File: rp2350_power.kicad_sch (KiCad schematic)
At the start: 24 parts, among them J1 TYPE-C 16PLT-H10.0, U2 LM2596S-3.3, U6 XXL1509-5.0

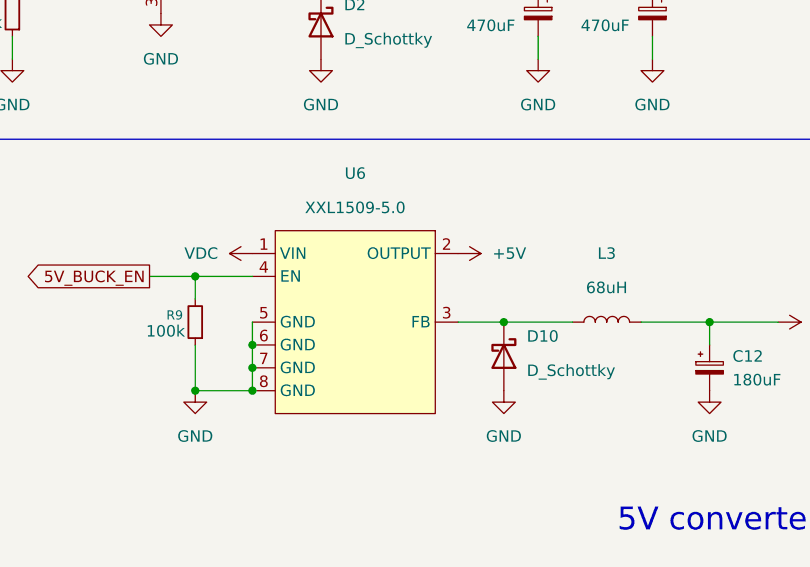
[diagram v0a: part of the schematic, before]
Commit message: fixed wrong wiring of 5V regulator for rp mcu + added all usb a ports
Signed-off-by: Toby Cm <toby@vsus.app>
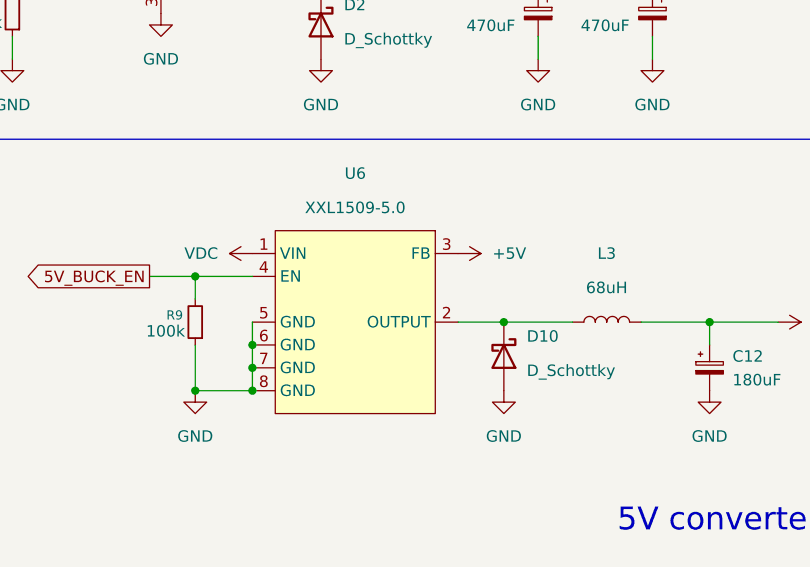
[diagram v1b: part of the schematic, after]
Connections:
- net +5V: now also U6.3 (FB); no longer U6.2 (OUTPUT)
- net at D10.1 (K), L3.1: now also U6.2 (OUTPUT); no longer U6.3 (FB)

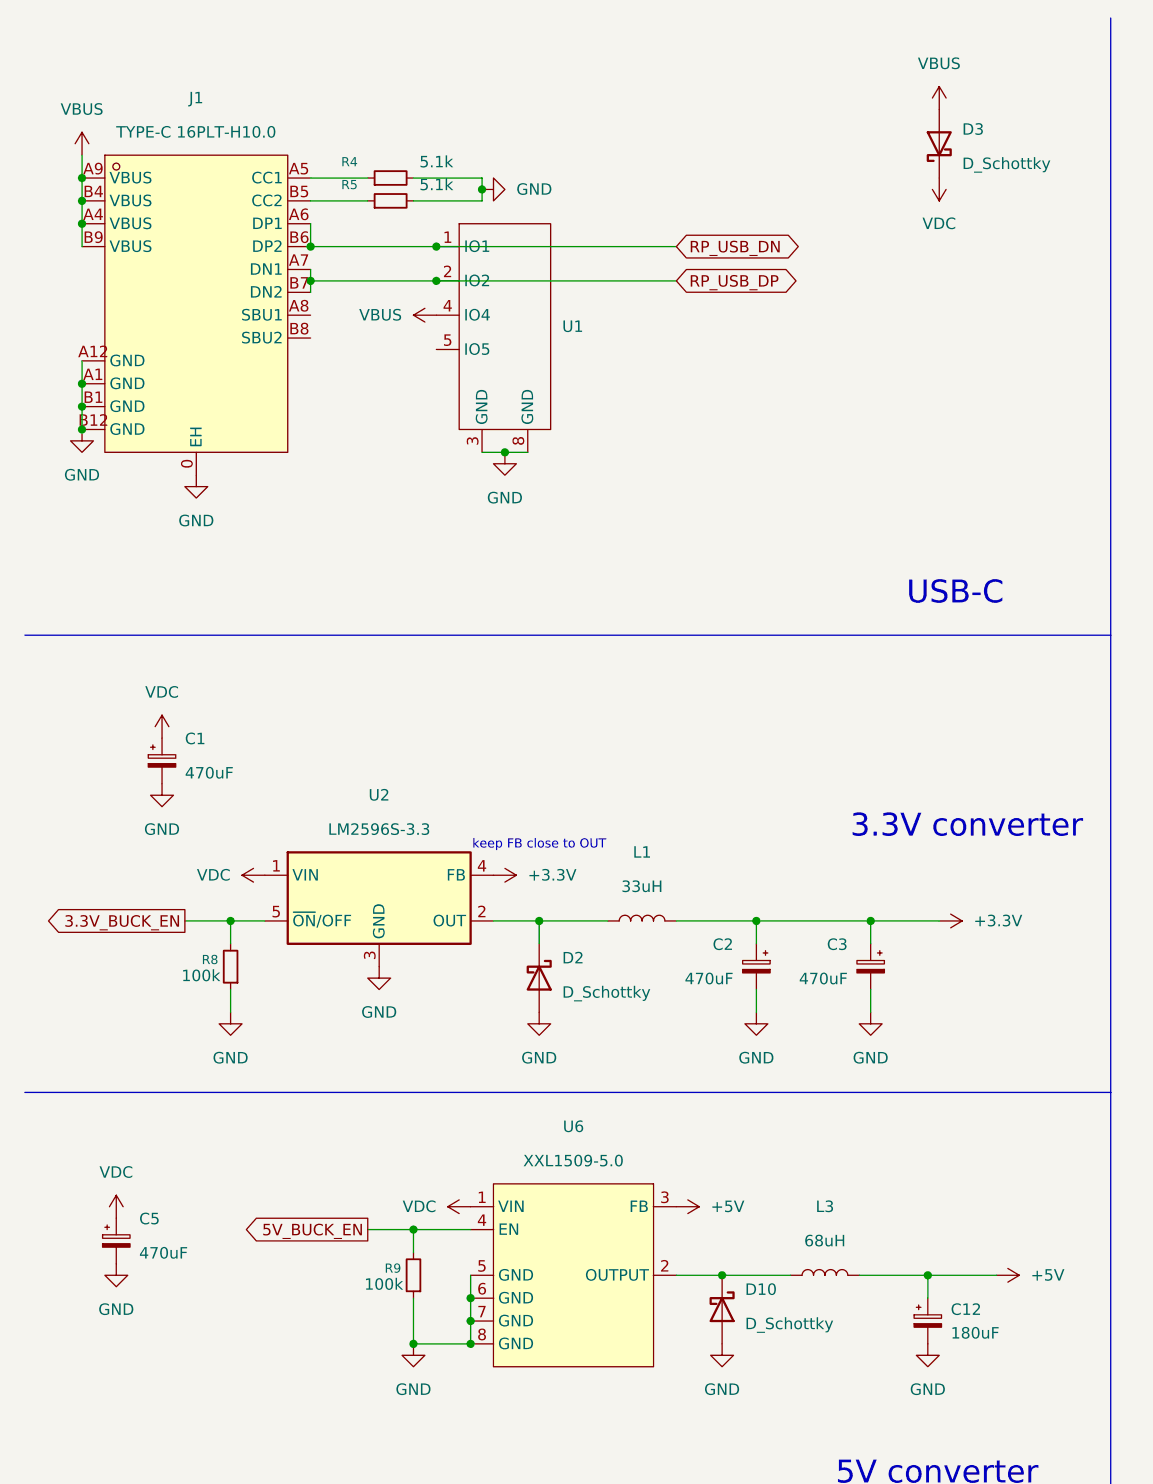
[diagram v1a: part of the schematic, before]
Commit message: gave up on single board, gonna make small modules
Signed-off-by: Toby Cm <toby@vsus.app>
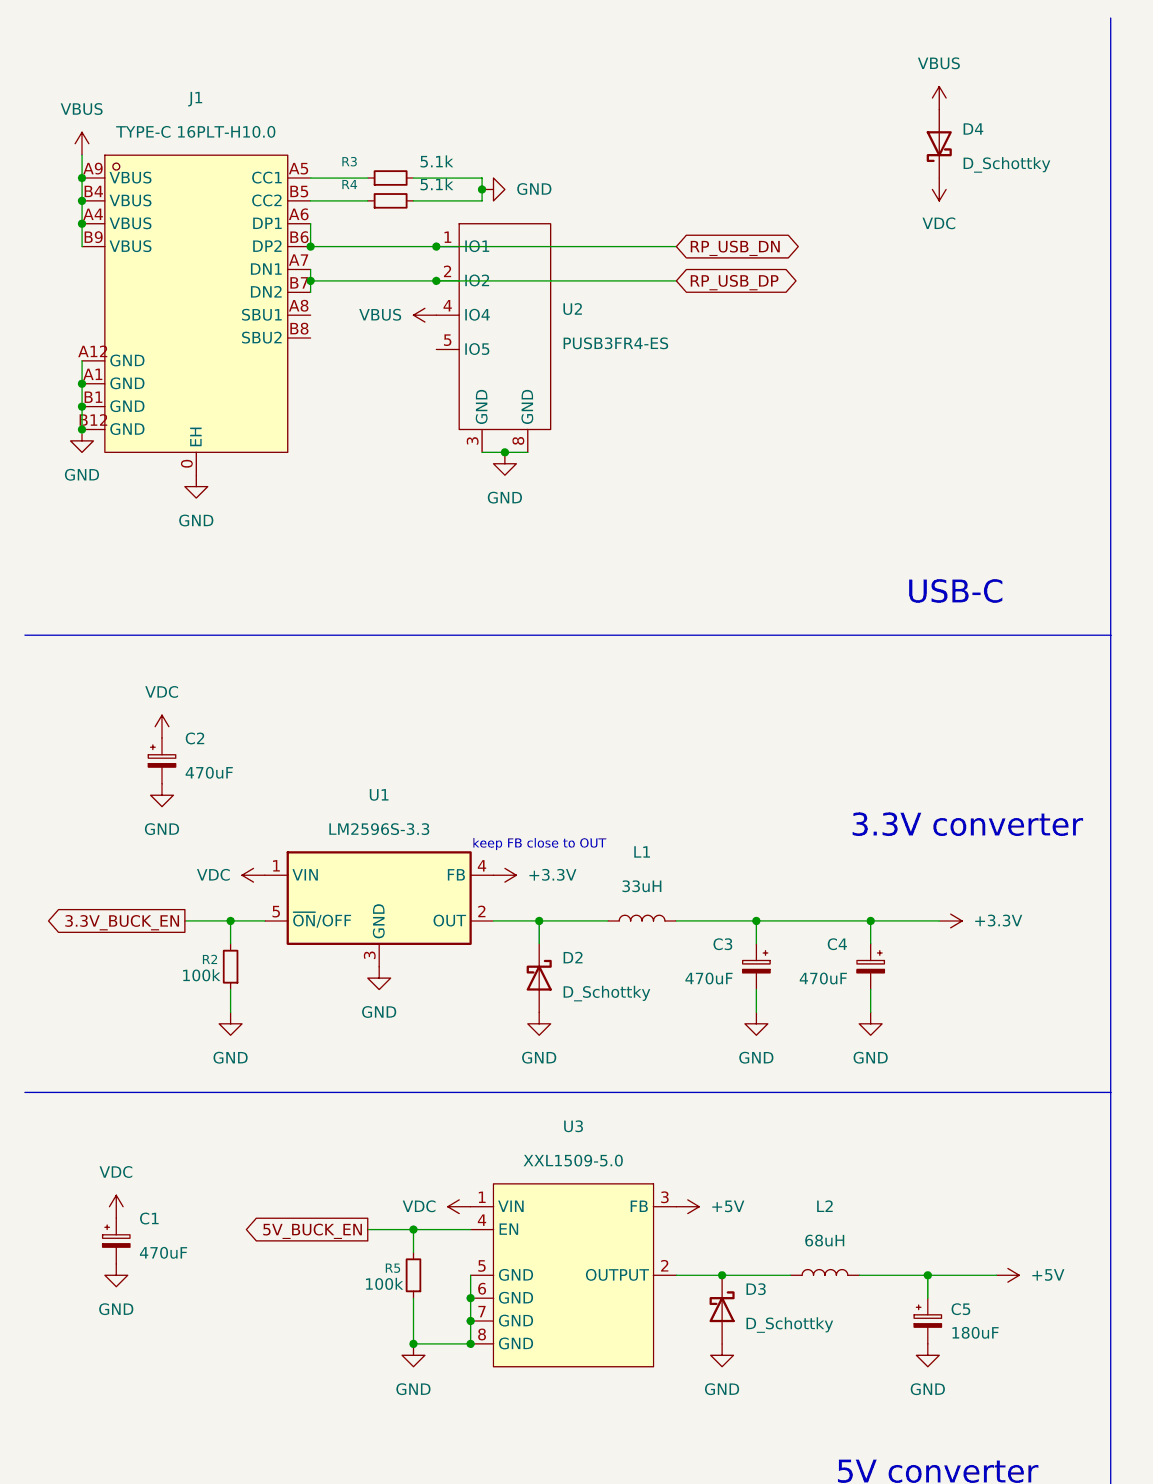
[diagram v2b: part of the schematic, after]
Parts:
- C1: renamed from C5; footprint (none) -> Capacitor_THT:CP_Radial_D17.0mm_P7.50mm
- C2: renamed from C1; footprint (none) -> Capacitor_THT:CP_Radial_D17.0mm_P7.50mm
- C3: renamed from C2; footprint (none) -> Capacitor_THT:CP_Radial_D17.0mm_P7.50mm
- C4: renamed from C3; footprint (none) -> Capacitor_THT:CP_Radial_D17.0mm_P7.50mm
- C5: renamed from C12; footprint (none) -> Capacitor_THT:CP_Radial_D8.0mm_P5.00mm
- D2: footprint (none) -> Diode_SMD:D_SMB_Handsoldering
- D3: renamed from D10; footprint (none) -> Diode_SMD:D_SMB_Handsoldering
- D4: renamed from D3; footprint (none) -> Diode_SMD:D_SMB_Handsoldering
- L2: renamed from L3; footprint (none) -> easyeda2kicad:IND-SMD_L8.0-W8.0-1
- R2: renamed from R8; footprint (none) -> Resistor_SMD:R_0402_1005Metric_Pad0.72x0.64mm_HandSolder
- R3: renamed from R4; footprint (none) -> Resistor_SMD:R_0402_1005Metric_Pad0.72x0.64mm_HandSolder
- R4: renamed from R5; footprint (none) -> Resistor_SMD:R_0402_1005Metric_Pad0.72x0.64mm_HandSolder
- R5: renamed from R9; footprint (none) -> Resistor_SMD:R_0402_1005Metric_Pad0.72x0.64mm_HandSolder
- U2: renamed from U1; value ~ -> PUSB3FR4-ES; footprint (none) -> Package_DFN_QFN:Diodes_UDFN-10_1.0x2.5mm_P0.5mm
- renumbered U2 to U1, U6 to U3
